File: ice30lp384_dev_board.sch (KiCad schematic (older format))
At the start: 15 parts, among them J1 Conn_01x08, J2 Conn_01x08, U1 MIC5365-1.2YC5-TR, U2 ECS-TXO-2520-33-250-AN-TR, U3 ICE40LP384-SG32, U4 W25X10CLSNIG

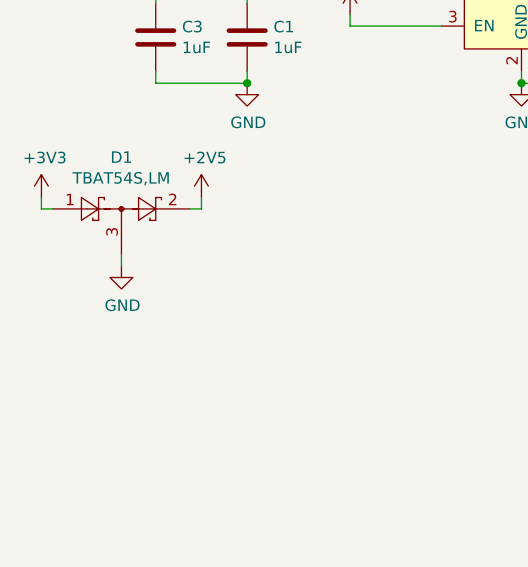
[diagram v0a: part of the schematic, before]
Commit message: Removed ground connection from 2.5V Diode
Updated files to change ground connection to no-connection for 2.5v diode. v1.0 boards have cut traces to prevent short to ground.
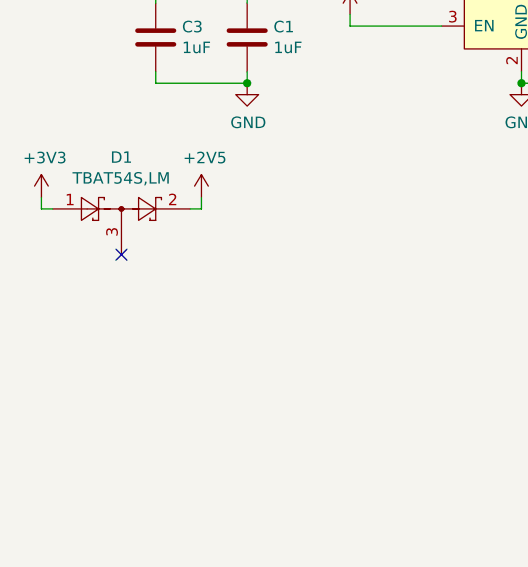
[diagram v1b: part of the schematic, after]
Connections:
- net GND: no longer D1.3
- no-connect marks 1 -> 2
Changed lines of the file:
@@
 	1750 2050 1700 2050
-$Comp
-L power:GND #PWR02
-U 1 1 5F7D0395
-P 1400 2300
-F 0 "#PWR02" H 1400 2050 50  0001 C CNN
-F 1 "GND" H 1405 2127 50  0000 C CNN
-F 2 "" H 1400 2300 50  0001 C CNN
-F 3 "" H 1400 2300 50  0001 C CNN
-	1    1400 2300
-	1    0    0    -1
-$EndComp
-Wire Wire Line
-	1400 2250 1400 2300
 $Comp
 L power:+2V5 #PWR06
@@
 	1950 1450 1950 1500
 Connection ~ 1950 1500
+NoConn ~ 1400 2250
 $EndSCHEMATC
